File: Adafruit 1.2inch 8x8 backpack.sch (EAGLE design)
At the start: 15 parts, among them CN1 1X4-CLEANBIG

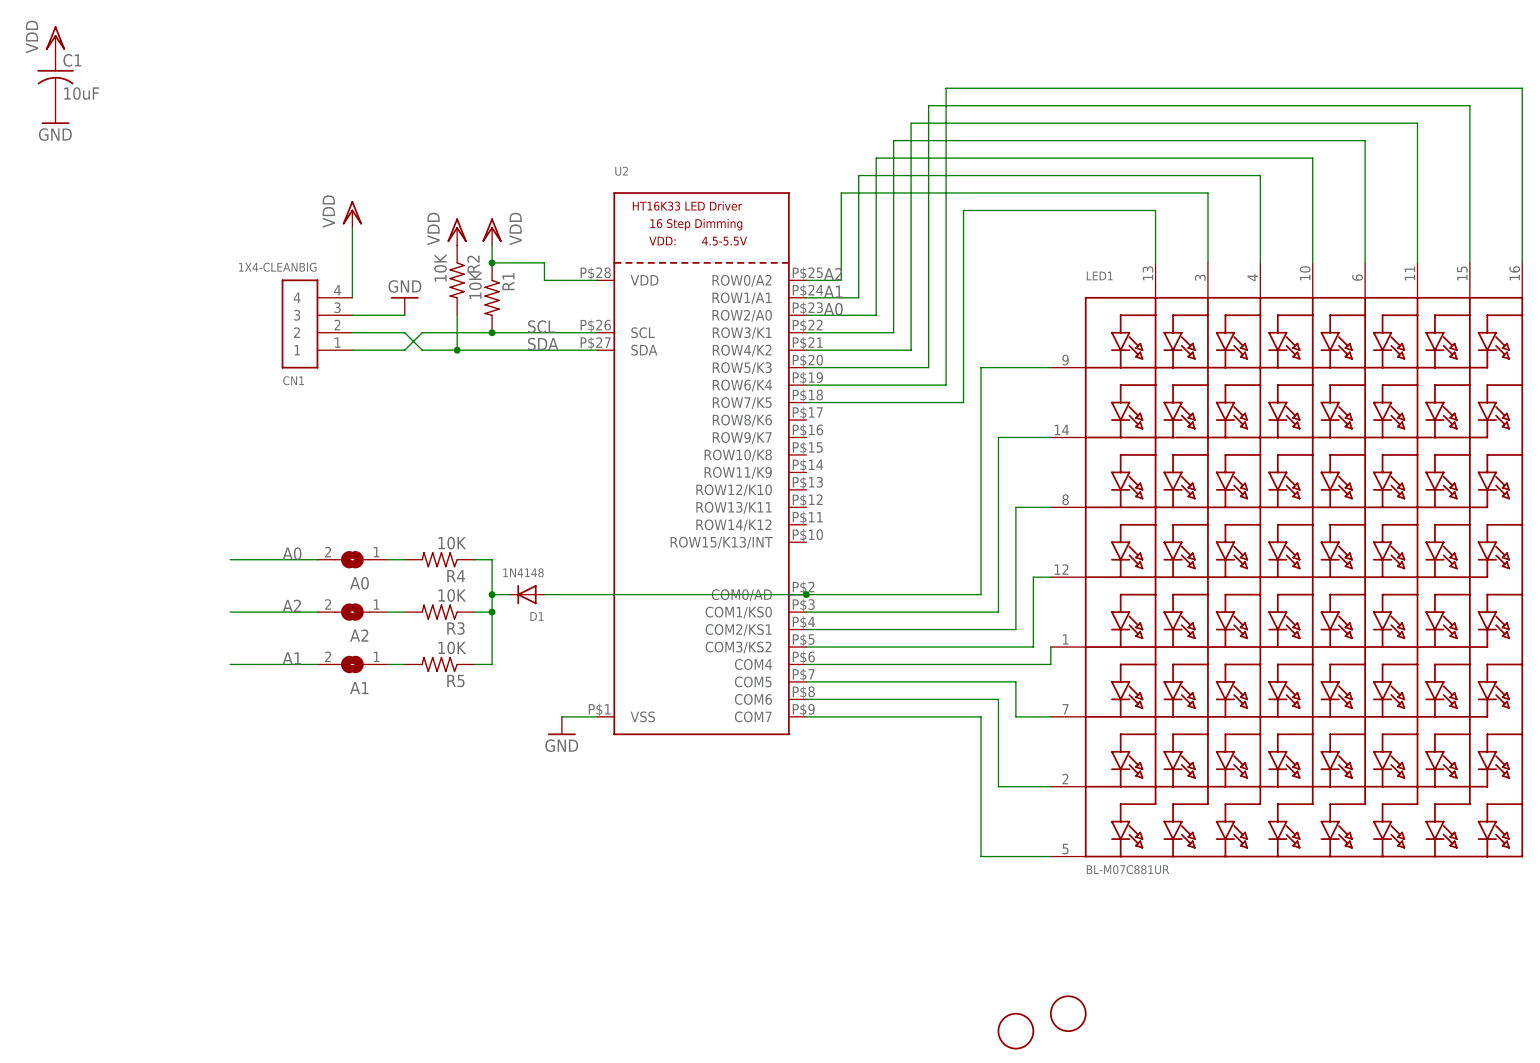
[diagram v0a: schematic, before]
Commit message: Update 1.2-inch 8x8 backpack files
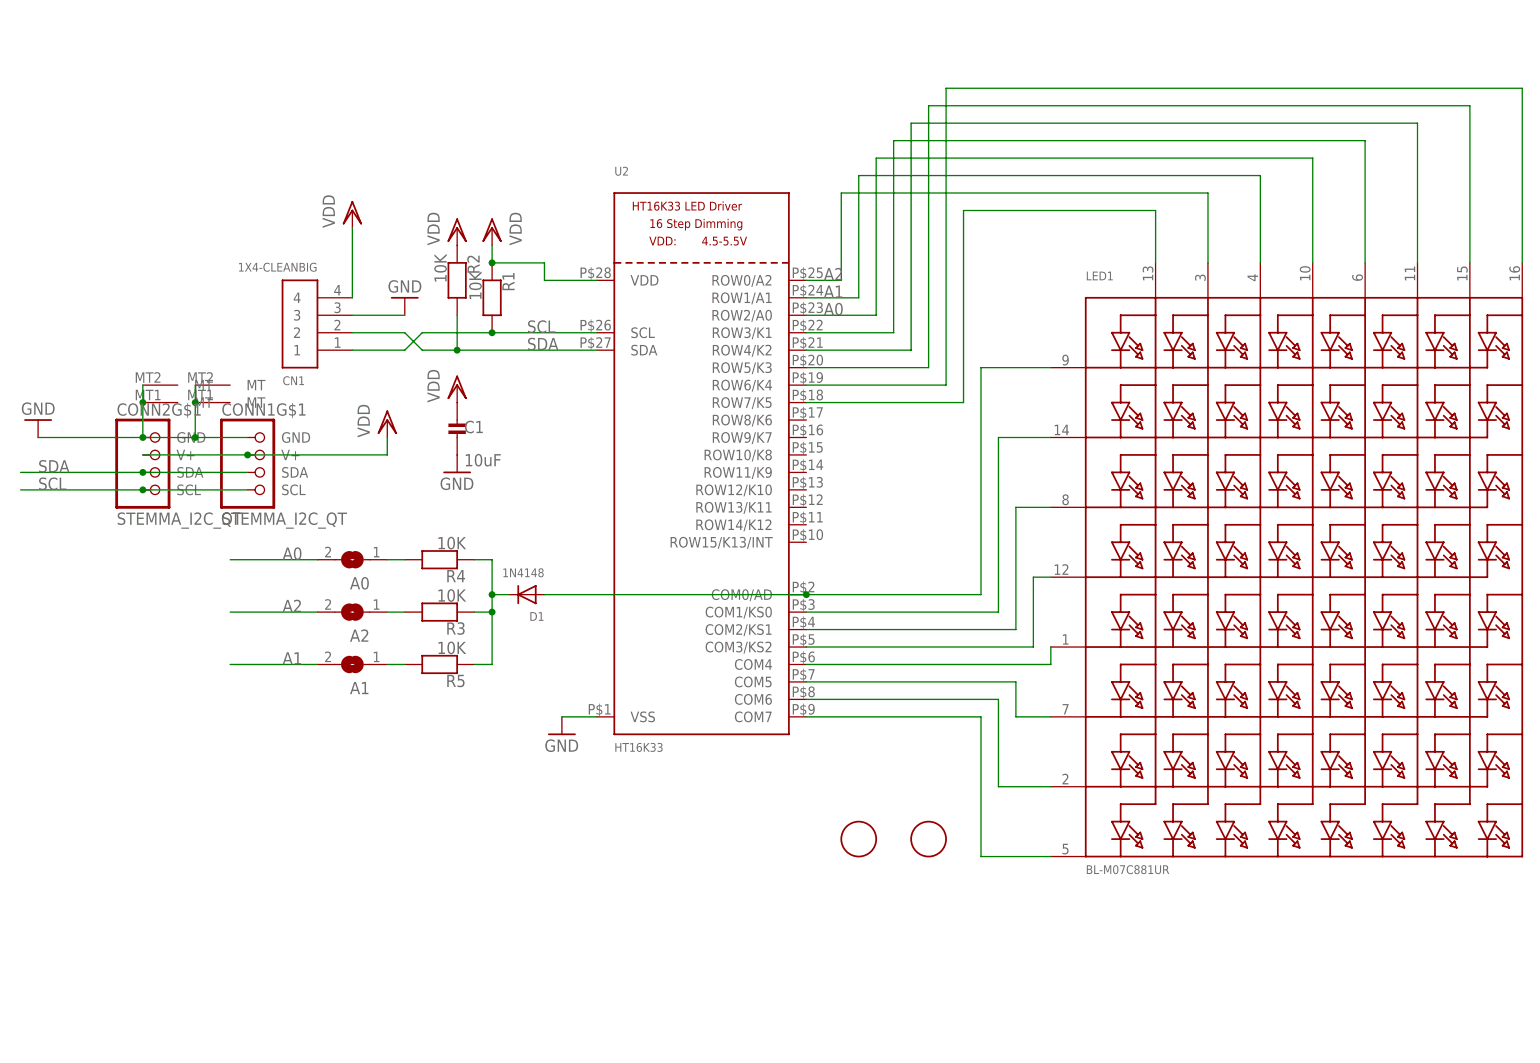
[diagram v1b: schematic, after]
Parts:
- added CONN1, CONN2: STEMMA_I2C_QT, adafruit_electromech:STEMMA_I2C_QT
- C1: device rcl:C-USC0805 -> microbuilder:CAP_CERAMIC0805-NOOUTLINE
- D1: device adafruit:DIODESOD-323F -> microbuilder:DIODESOD-323
- LED1: device microbuilder:DISP_SEGMENT_8X8_ROWCATHODEM12A881UR -> adafruit_display:DISP_SEGMENT_8X8_ROWCATHODEM12A881UR
- R1, R2, R3, R4, R5: device adafruit:R-US_R0805 -> microbuilder:RESISTOR_0603_NOOUT
- U2: value (none) -> HT16K33; device microbuilder:HT16K33_SOP28 -> adafruit_display:HT16K33_SOP28
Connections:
- net GND: now also CONN1G$1.GND, CONN1G$2.MT, CONN1G$3.MT, CONN2G$1.GND, CONN2G$2.MT, CONN2G$3.MT
- net SCL: now also CONN1G$1.SCL, CONN2G$1.SCL
- net SDA: now also CONN1G$1.SDA, CONN2G$1.SDA
- net VDD: now also CONN1G$1.V+, CONN2G$1.V+
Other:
- moved on the sheet: C1
